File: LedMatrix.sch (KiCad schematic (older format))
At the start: 28 parts, among them IC1 ATMEGA328P-A, P1 FTDI, P2 SYNC_OUT, P3 ICSP, SW1 SW_PUSH, SW2 SWITCH_INV, U1 74HC238, U2 M54562FP, U3 MCP1700-3302, U4 TLC5917, U5 ADXL345, X1 8Mhz

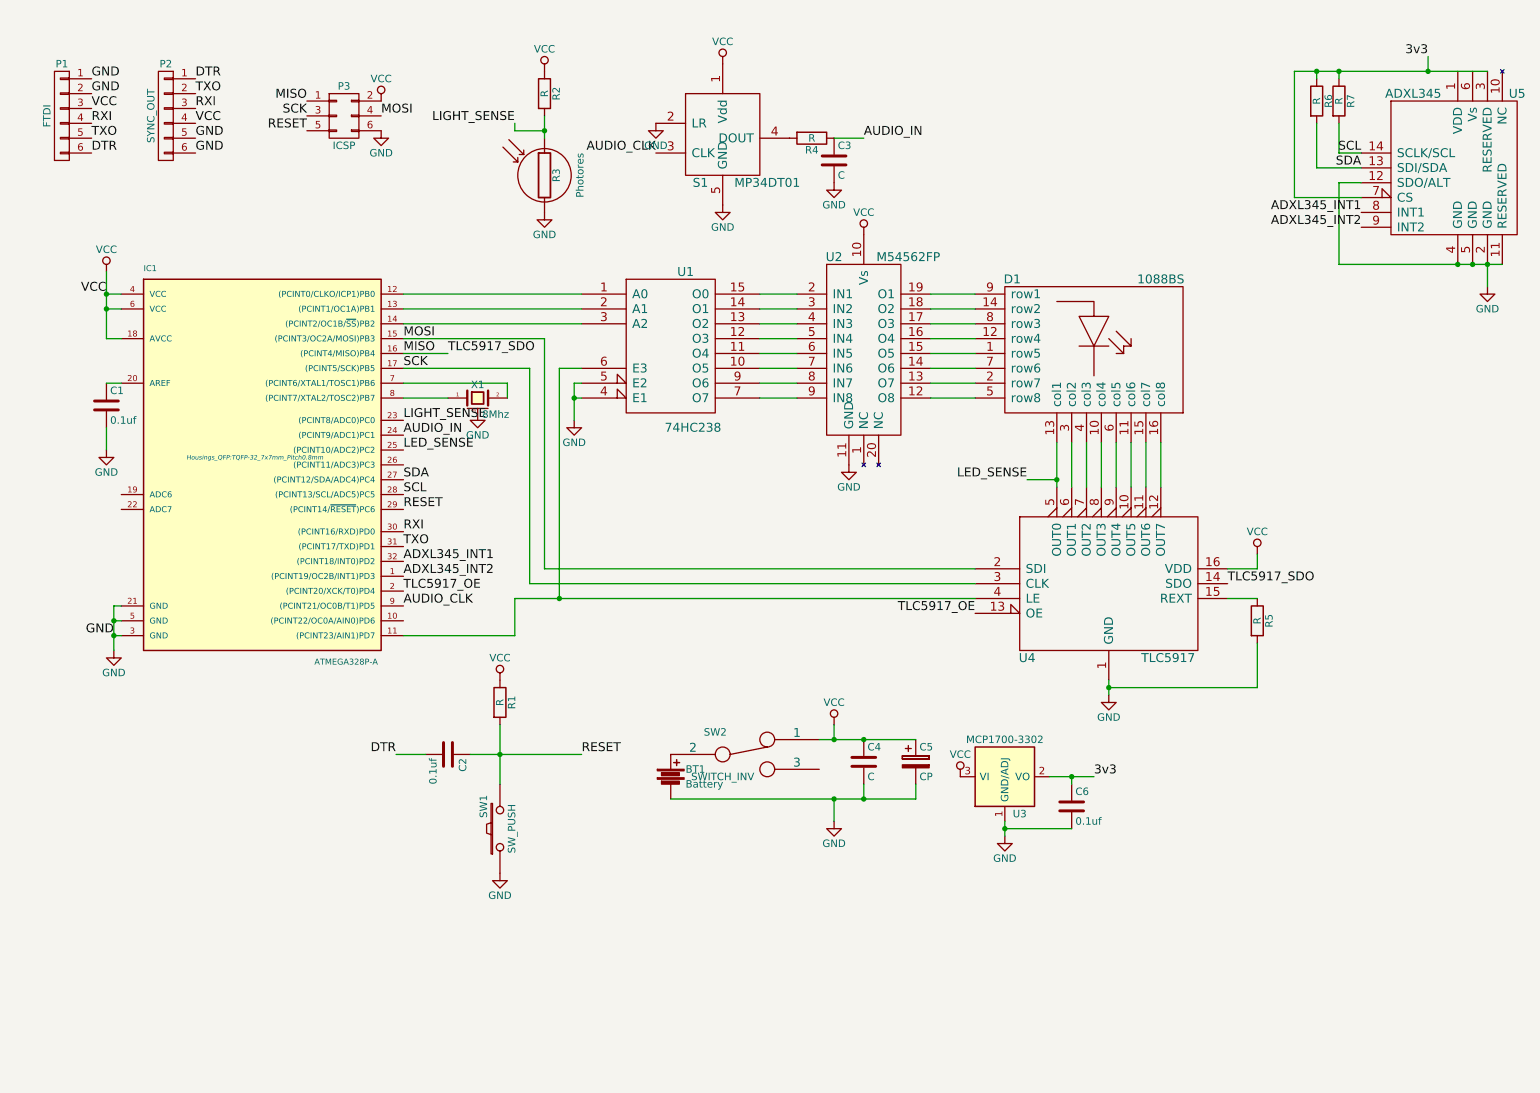
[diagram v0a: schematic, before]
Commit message: Update the LED control program
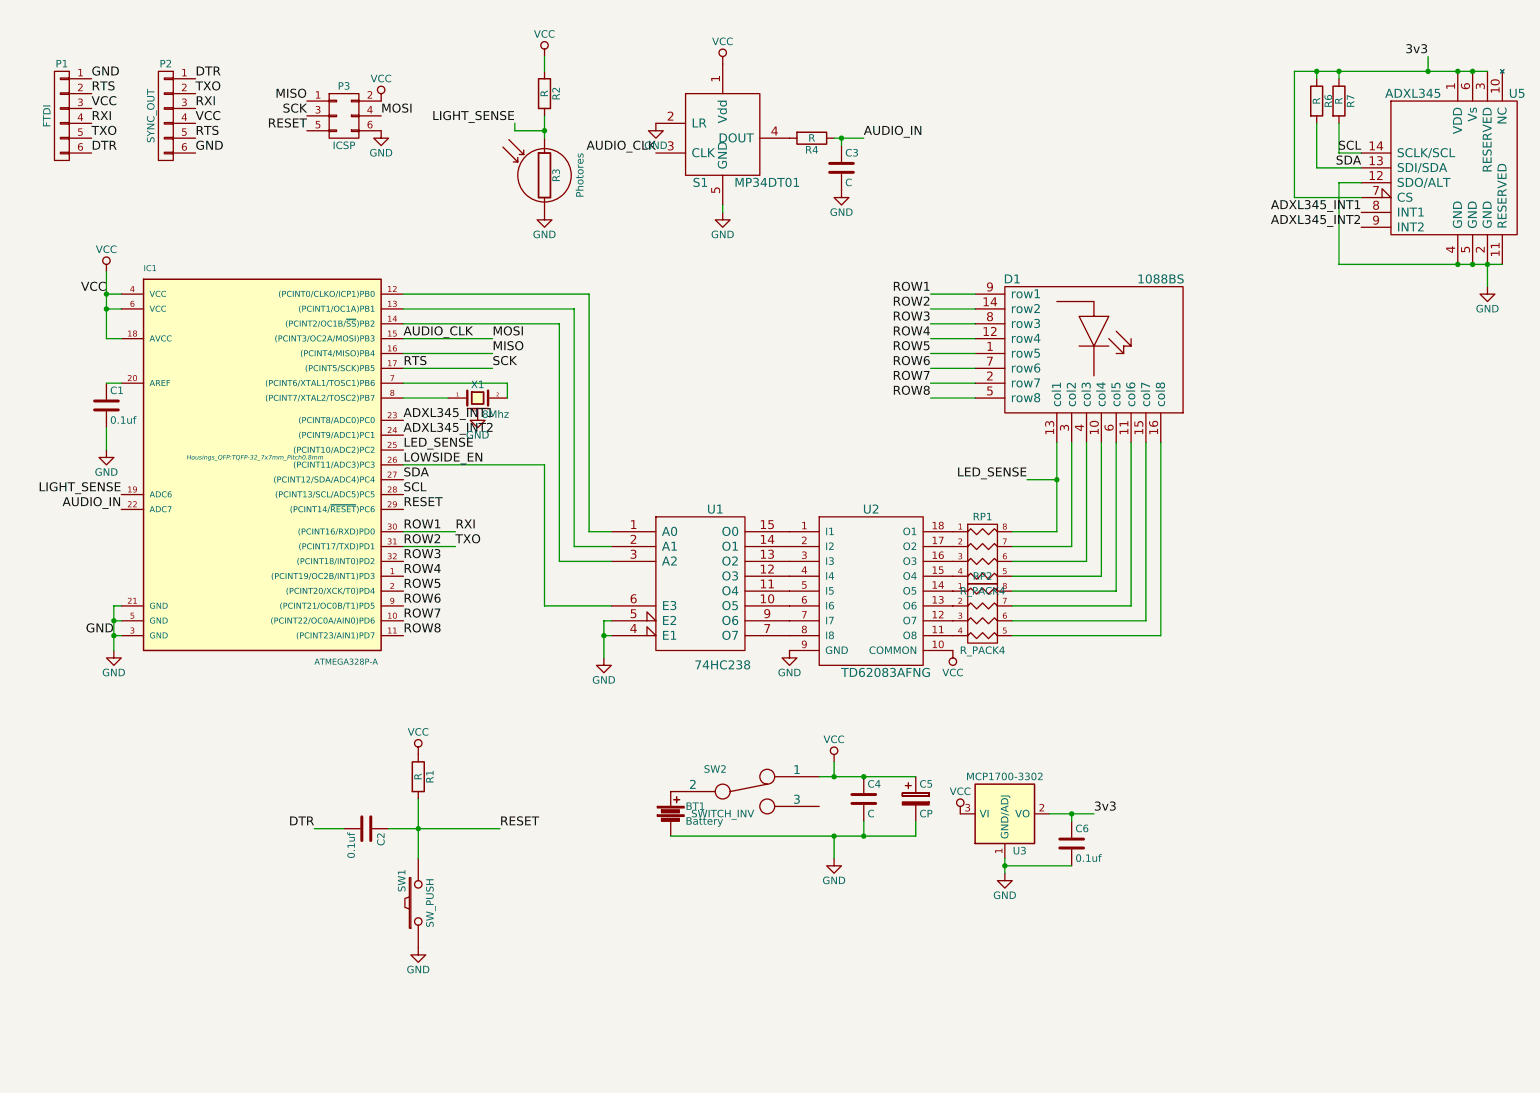
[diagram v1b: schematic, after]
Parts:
- removed R5: R, Resistors_SMD:R_0805, symbol R
- removed U2: M54562FP, Housings_SOIC:SOIC-20_7.5x12.8mm_Pitch1.27mm, symbol M54562FP
- removed U4: TLC5917, Housings_SSOP:TSSOP-16_4.4x5mm_Pitch0.65mm, symbol TLC5917
- added RP1, RP2: R_PACK4, Resistors_SMD:R_Array_Convex_4x0402, symbol R_PACK4
- added U2: TD62083AFNG, SSOP18:TSSOP-14_4.4x5mm_Pitch0.65mm, symbol TD62083AFNG
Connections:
- net MOSI is gone; now on net AUDIO_CLK: IC1.15 ((PCINT3/OC2A/MOSI)PB3), P3.4 (P4)
- net RXI is gone; now on net ROW1: IC1.30 ((PCINT16/RXD)PD0), P1.4 (P4), P2.3 (P3)
- net TLC5917_OE is gone; now on net ROW5: IC1.2 ((PCINT20/XCK/T0)PD4)
- net TXO is gone; now on net ROW2: IC1.31 ((PCINT17/TXD)PD1), P1.5 (P5), P2.2 (P2)
- net 3v3: now also U5.1 (VDD), U5.6 (Vs)
- net ADXL345_INT1: now also IC1.23 ((PCINT8/ADC0)PC0); no longer IC1.32 ((PCINT18/INT0)PD2)
- net ADXL345_INT2: now also IC1.24 ((PCINT9/ADC1)PC1); no longer IC1.1 ((PCINT19/OC2B/INT1)PD3)
- net AUDIO_CLK: no longer IC1.9 ((PCINT21/OC0B/T1)PD5)
- net AUDIO_IN: now also IC1.22 (ADC7); no longer IC1.24 ((PCINT9/ADC1)PC1)
- net GND: now also U2.9 (GND); no longer P1.2 (P2), P2.5 (P5)
- net LED_SENSE: now also RP1.8 (R1)
- net LIGHT_SENSE: now also IC1.19 (ADC6); no longer IC1.23 ((PCINT8/ADC0)PC0)
- net VCC: now also U2.10 (COMMON)
- net at U1.10 (O5): now also U2.6 (I6)
- net at U1.11 (O4): now also U2.5 (I5)
- net at U1.12 (O3): now also U2.4 (I4)
- net at U1.13 (O2): now also U2.3 (I3)
- net at U1.14 (O1): now also U2.2 (I2)
- net at U1.15 (O0): now also U2.1 (I1)
- net LOWSIDE_EN: now reaches U1.6 (E3)
- net LOWSIDE_EN: now also IC1.26 ((PCINT11/ADC3)PC3); no longer IC1.11 ((PCINT23/AIN1)PD7)
- net at U1.7 (O7): now also U2.8 (I8)
- net at U1.9 (O6): now also U2.7 (I7)
- net ROW7: now reaches IC1.10 ((PCINT22/OC0A/AIN0)PD6)
- net ROW7: now also D1.2 (row7)
- net at D1.11 (col6): now also RP2.7 (R2)
- net at D1.15 (col7): now also RP2.6 (R3)
- net at D1.16 (col8): now also RP2.5 (R4)
- net at D1.3 (col2): now also RP1.7 (R2)
- net at D1.4 (col3): now also RP1.6 (R3)
- net at D1.10 (col4): now also RP1.5 (R4)
- net at D1.6 (col5): now also RP2.8 (R1)
- net ROW5: now reaches D1.1 (row5)
- net ROW4: now reaches D1.12 (row4)
- net ROW4: now also IC1.1 ((PCINT19/OC2B/INT1)PD3)
- net ROW2: now reaches D1.14 (row2)
- net ROW8: now reaches D1.5 (row8)
- net ROW8: now also IC1.11 ((PCINT23/AIN1)PD7)
- net ROW6: now reaches D1.7 (row6)
- net ROW6: now also IC1.9 ((PCINT21/OC0B/T1)PD5)
- net ROW3: now reaches D1.8 (row3)
- net ROW3: now also IC1.32 ((PCINT18/INT0)PD2)
- net ROW1: now reaches D1.9 (row1)
- net SCK renamed RTS
- net RTS: now also P1.2 (P2), P2.5 (P5)
- new net: RP2.4 (P4), U2.11 (O8)
- new net: RP2.3 (P3), U2.12 (O7)
- new net: RP2.2 (P2), U2.13 (O6)
- new net: RP2.1 (P1), U2.14 (O5)
- new net: RP1.4 (P4), U2.15 (O4)
- new net: RP1.3 (P3), U2.16 (O3)
- new net: RP1.2 (P2), U2.17 (O2)
- new net: RP1.1 (P1), U2.18 (O1)
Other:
- moved on the sheet: BT1, C2, C3, C4, C5, C6, R1, SW1, SW2, U1, U3

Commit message: Use flash memory for animation
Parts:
- added R5: 10k, Resistors_SMD:R_0805, symbol R
- added U4: PNJ4K01F, pnj4k01f:KPTFTN6K0001, symbol PNJ4K01F
- C3: value C -> 10nf
- C4: value C -> 0.1uf
- C5: value CP -> 10uf
- R1, R4: value R -> 10k
- R2: value R -> 100k
- R6, R7: value R -> 2k
- RP1, RP2: footprint Resistors_SMD:R_Array_Convex_4x0402 -> Resistors_SMD:R_Array_Concave_4x0603
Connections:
- net 3v3: now also S1.1 (Vdd)
- net GND: now also R2.2, R5.2, U4.2 (GND), U4.3 (GND), U4.4 (GND), U4.5 (GND); no longer R3.2
- net LIGHT_SENSE: now also R2.1, R3.2, U4.6 (OUT); no longer R2.2, R3.1
- net LOWSIDE_EN: now also R5.1
- net VCC: now also R3.1, U4.1 (Vcc); no longer R2.1, S1.1 (Vdd)
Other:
- moved on the sheet: C3, R2, R3, R4, S1

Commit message: Add francis and northy mods
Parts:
- removed P1: FTDI, Pin_Headers:Pin_Header_Straight_1x06, symbol CONN_01X06
- removed P2: SYNC_OUT, Pin_Headers:Pin_Header_Straight_1x06, symbol CONN_01X06
- removed R3: Photores, Discret:R1, symbol Photores
- removed S1: MP34DT01, MP34DT01:MP34DT01, symbol MP34DT01
- removed SW2: SWITCH_INV, 1P2T:1P2T_SideSwitch, symbol SWITCH_INV
- removed U3: MCP1700-3302, Housings_SOT-23_SOT-143_TSOT-6:SOT-23, symbol AP1117D33
- removed U4: PNJ4K01F, pnj4k01f:KPTFTN6K0001, symbol PNJ4K01F
- added C7: 1uf, Capacitors_SMD:C_0603, symbol C
- added D2: D_Schottky, Diodes_SMD:SMA_Standard, symbol D_Schottky
- added M1: 3729Mic, 3729Mic:3729Mic, symbol 3729Mic
- added P0, P1: CONN_01X04, Pin_Headers:Pin_Header_Straight_1x04, symbol CONN_01X04
- added P2: USB_OTG, Molex475890001:47589-0001, symbol USB_OTG
- added R3: 5.1k, Resistors_SMD:R_0603, symbol R
- added R8: 100k, Resistors_SMD:R_0603, symbol R
- added R9: 10k, Resistors_SMD:R_0603, symbol R
- added U3: CH340T, Housings_SSOP:SSOP-20_5.3x7.2mm_Pitch0.65mm, symbol CH340T
- added U4: TPCP8405, ps_8:PS-8, symbol TPCP8405
- added U6: APDS-9900, ADPS-9900:ADPS-9900, symbol APDS-9900
- added U7: AP1117D30, TO_SOT_Packages_SMD:SOT-223, symbol AP1117D33
- added X2: 12Mhz, CSTCE8M:CSTCE8M00G52, symbol CRYSTAL_SMD
- C1, C2, C4, C6: footprint Capacitors_SMD:C_0805 -> Capacitors_SMD:C_0603
- C3: value 10nf -> 0.1uf; footprint Capacitors_SMD:C_0805 -> Capacitors_SMD:C_0603
- IC1: footprint Housings_QFP:TQFP-32_7x7mm_Pitch0.8mm -> Housings_DFN_QFN:QFN-32-1EP_5x5mm_Pitch0.5mm
- R1, R4, R5, R6, R7: footprint Resistors_SMD:R_0805 -> Resistors_SMD:R_0603
- R2: value 100k -> 10k; footprint Resistors_SMD:R_0805 -> Resistors_SMD:R_0603
- SW1: footprint SideButton:SidePushButton -> SKSCLCE010:SKSCLCE010
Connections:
- net AUDIO_IN: now also M1.4 (OUT); no longer C3.1, R4.1
- net GND: now also C3.1, C7.2, M1.2 (GND), M1.3 (GND), P0.4 (P4), P1.4 (P4), P2.5 (GND), U3.8 (GND), U4.1, U6.6 (GND), U7.1 (GND/ADJ), X2.3 (case); no longer C3.2, R2.2, SW1.1
- net LED_SENSE: now also IC1.19 (ADC6); no longer IC1.25 ((PCINT10/ADC2)PC2)
- net MISO: now also P0.2 (P2)
- net RESET: no longer SW1.2
- net ROW1: now also R2.1
- net ROW2: now also R3.1
- net SCL: now also U6.7 (SCL)
- net SDA: now also U6.1 (SDA)
- net VCC: now also R6.1, R7.1, U5.1 (VDD), U5.3 (RESERVED), U5.6 (Vs), U5.7 (CS), D2.1 (K), M1.1 (Vcc), P0.1 (P1), P1.1 (P1), R9.1, U4.5, U4.6, U6.5 (LED_A), U6.8 (VDD); no longer C4.1, C5.1
- net at R4.2: now also R8.1, U4.4, U4.7, U4.8
- net at BT1.1: now also C4.1, C5.1, R4.1, U4.3
- removed net 3v3: C6.1, R6.1, R7.1, U5.1 (VDD), U5.3 (RESERVED), U5.6 (Vs), U5.7 (CS)
- net AUDIO_CLK renamed MOSI
- net MOSI: now also P1.2 (P2)
- net DTR: no longer names the net of C2.2
- net DTR: now also U3.15 (DTR)
- removed net LIGHT_SENSE: IC1.19 (ADC6), R2.1
- net RTS renamed SCK
- net SCK: now also P0.3 (P3), P1.3 (P3)
- new net: C6.1, D2.2 (A), U7.2 (VO)
- new net: U3.10 (XO), X2.2
- new net: R2.2, U3.3 (TXD)
- new net: R3.2, U3.4 (RXD)
- new net: C3.2, U3.5 (V3)
- new net: U3.9 (XI), X2.1
- new net: R9.2, SW1.2, U4.2
- new net: C7.1, R8.2, SW1.1
- new net: U6.3 (LDR), U6.4 (LED_K)
- new net 5V: P2.1 (VCC), U3.19 (VCC), U7.3 (VI)
- new net D+: P2.3 (D+), U3.6 (UD+)
- new net D-: P2.2 (D-), U3.7 (UD-)
- new net LIGHT_INT: IC1.25 ((PCINT10/ADC2)PC2), U6.2 (INT)
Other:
- moved on the sheet: C2, C4, C5, R1
